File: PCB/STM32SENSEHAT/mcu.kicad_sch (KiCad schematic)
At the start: 30 parts, among them J1 USB_B_Micro, J5 Conn_01x24_Pin, J6 Conn_01x10_Pin, J7 Conn_01x05_Pin, J8 Conn_01x24_Pin, SW1 SW_Push, U6 CAT24C256, U9 FT234XD-R, U9 STLINK_UCT

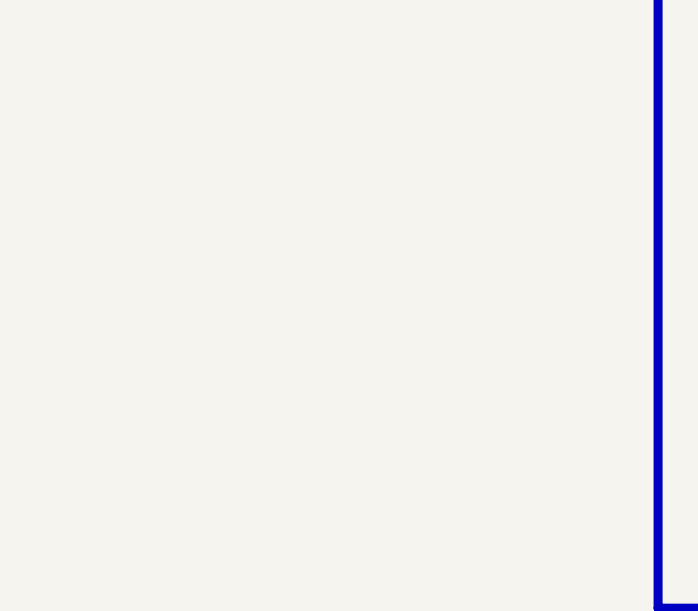
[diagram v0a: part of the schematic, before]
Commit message: OScillator added
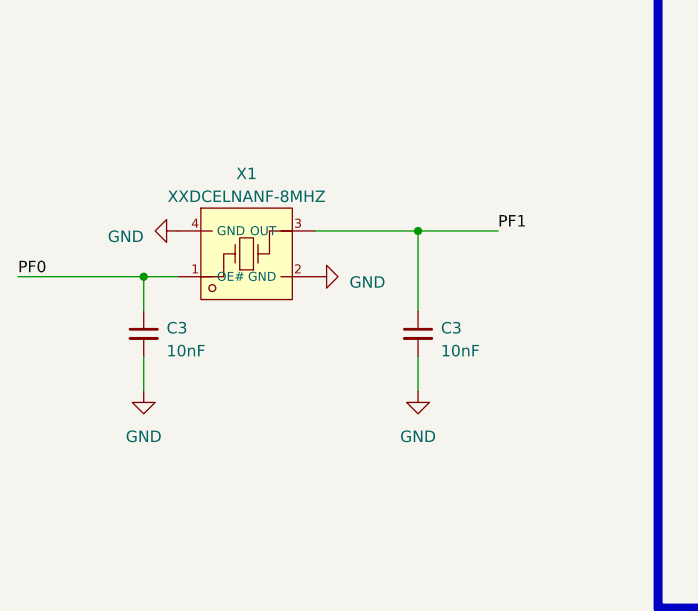
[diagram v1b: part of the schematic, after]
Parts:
- added C3 (x2): 10nF, Capacitor_SMD:C_0805_2012Metric, symbol Device:C_Small
- added X1: XXDCELNANF-8MHZ, JLCfootprint:OSC-SMD_4P-L3.2-W2.5-BL, symbol XXDCELNANF-8MHZ:XXDCELNANF-8MHZ
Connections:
- net GND: now also C3.2, C3.2, X1.2 (GND), X1.4 (GND)
- net PF0: now also C3.1, X1.1 (OE#)
- net PF1: now also C3.1, X1.3 (OUT)

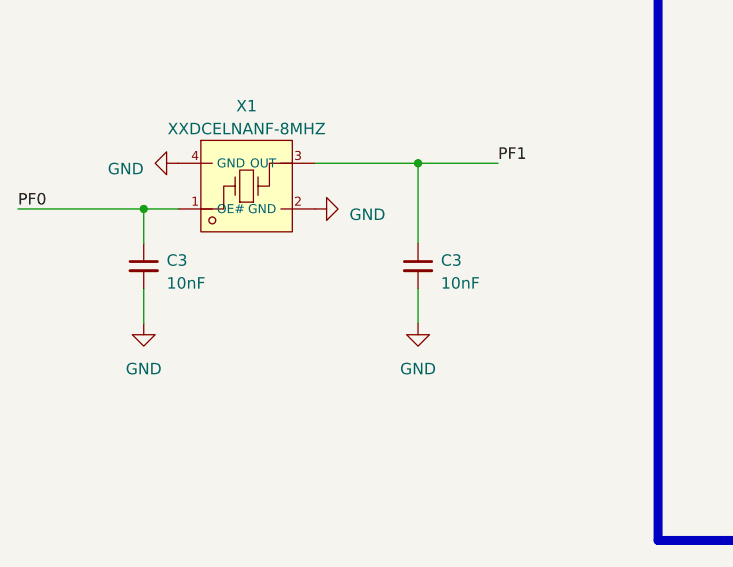
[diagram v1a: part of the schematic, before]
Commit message: Changed the value of the oscillator's capcitors to match the specified value in the datasheet
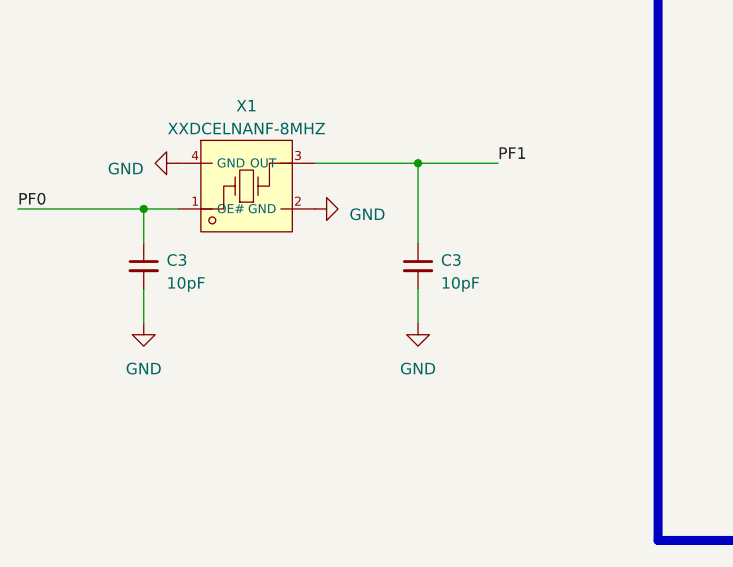
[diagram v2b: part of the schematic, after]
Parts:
- C3: value 10nF -> 10pF; footprint Capacitor_SMD:C_0805_2012Metric -> Capacitor_THT:C_Disc_D5.0mm_W2.5mm_P5.00mm
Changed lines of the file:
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@@
       (effects (font (size 1.27 1.27)) (justify left))
     )
-    (property "Value" "10nF" (at 78.74 67.9513 0)
+    (property "Value" "10pF" (at 78.74 67.9513 0)
       (effects (font (size 1.27 1.27)) (justify left))
     )
-    (property "Footprint" "Capacitor_SMD:C_0805_2012Metric" (at 76.2 66.04 0)
+    (property "Footprint" "Capacitor_THT:C_Disc_D5.0mm_W2.5mm_P5.00mm" (at 76.2 66.04 0)
       (effects (font (size 1.27 1.27)) hide)
     )
@@
       (effects (font (size 1.27 1.27)) (justify left))
     )
-    (property "Value" "10nF" (at 48.26 67.9513 0)
+    (property "Value" "10pF" (at 48.26 67.9513 0)
       (effects (font (size 1.27 1.27)) (justify left))
     )
-    (property "Footprint" "Capacitor_SMD:C_0805_2012Metric" (at 45.72 66.04 0)
+    (property "Footprint" "Capacitor_THT:C_Disc_D5.0mm_W2.5mm_P5.00mm" (at 45.72 66.04 0)
       (effects (font (size 1.27 1.27)) hide)
     )

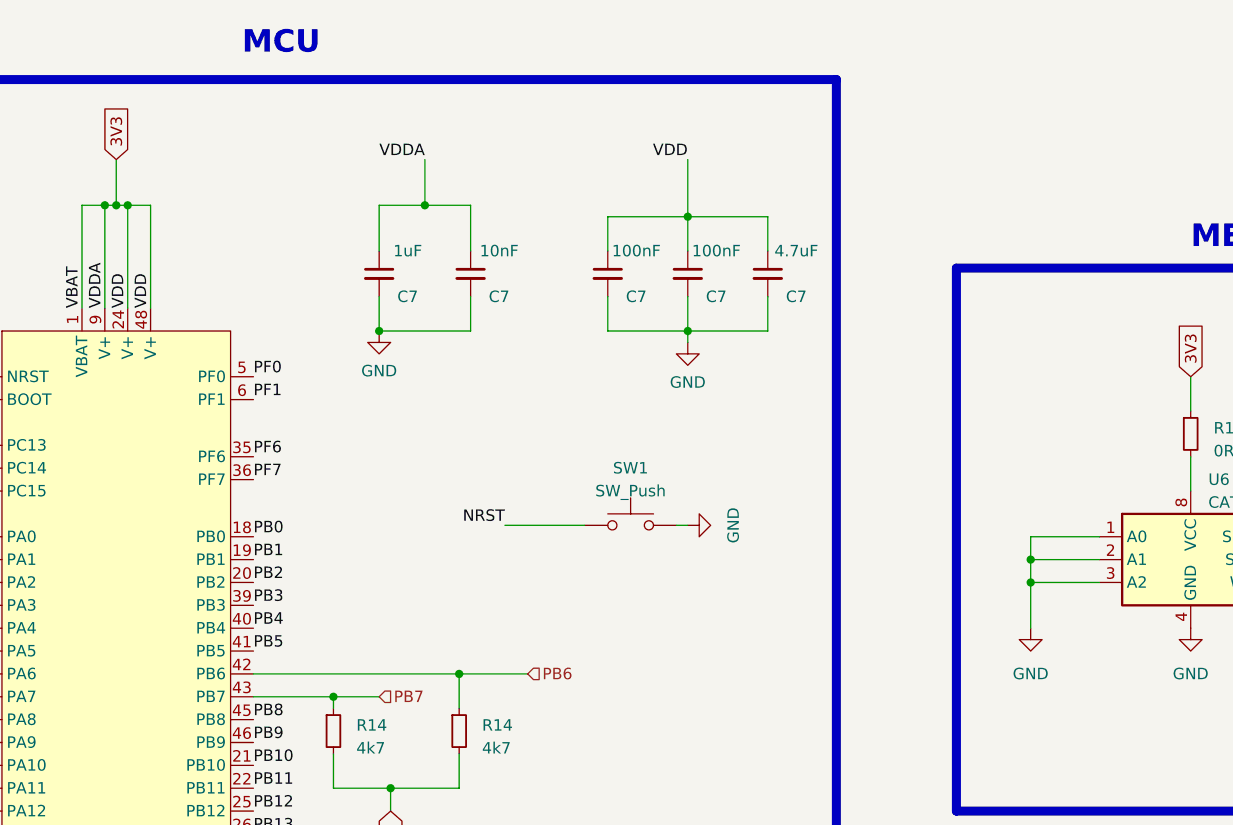
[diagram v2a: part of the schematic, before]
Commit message: Added capacitor paralle to NRST switch to mtigate parasitic effects
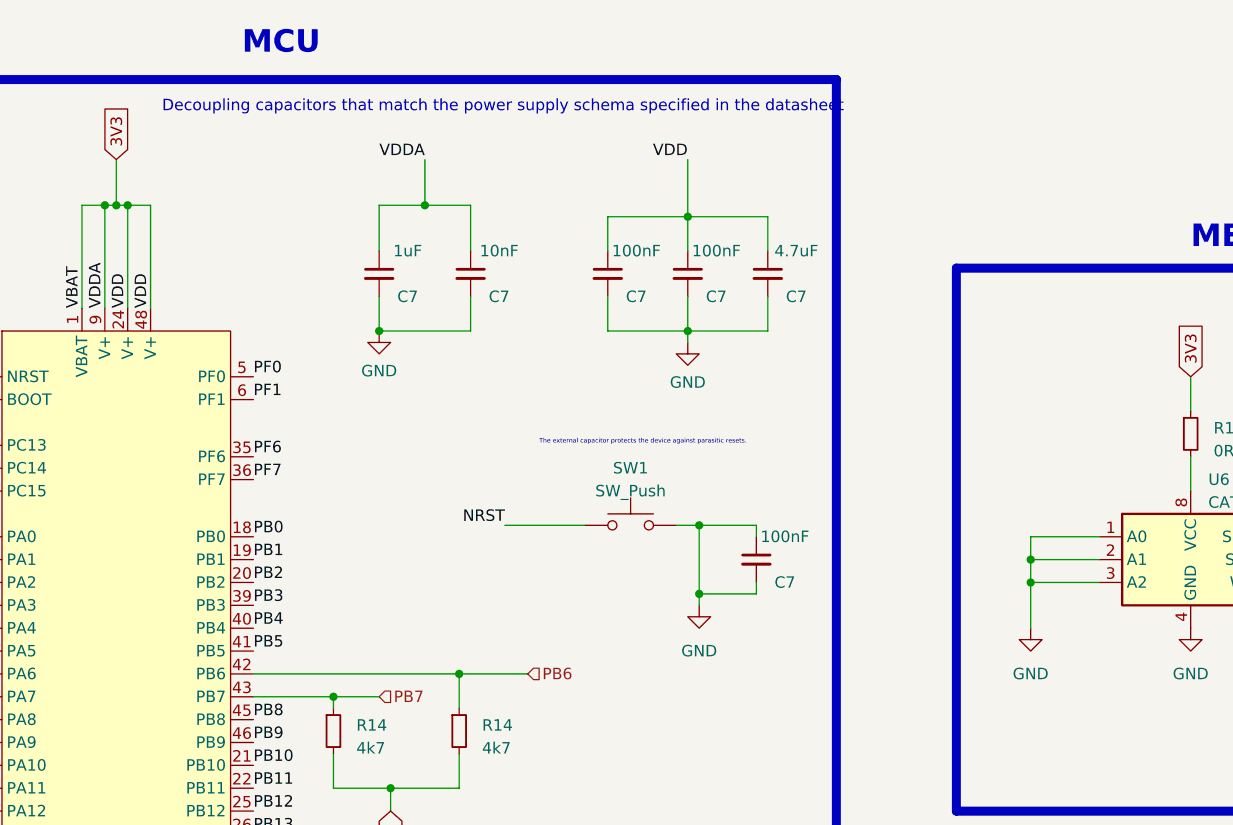
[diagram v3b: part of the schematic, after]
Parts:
- added C7: 100nF, Capacitor_THT:C_Disc_D5.0mm_W2.5mm_P5.00mm, symbol Device:C_Small
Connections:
- net GND: now also C7.1, C7.2
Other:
- note added: "Decoupling capacitors that match the power supply schema specified in the datasheet"
- note added: "The external capacitor protects the device against parasitic resets."
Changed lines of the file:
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@@
   (junction (at 228.6 119.38) (diameter 0) (color 0 0 0 0)
   )
+  (junction (at 293.37 69.85) (diameter 0) (color 0 0 0 0)
+  )
   (junction (at 330.2 76.2) (diameter 0) (color 0 0 0 0)
   )
@@
   (junction (at 330.2 73.66) (diameter 0) (color 0 0 0 0)
   )
+  (junction (at 293.37 77.47) (diameter 0) (color 0 0 0 0)
+  )
   (junction (at 228.6 34.29) (diameter 0) (color 0 0 0 0)
   )
@@
     (stroke (width 0) (type default))
   )
+  (wire (pts (xy 299.72 69.85) (xy 293.37 69.85))
+    (stroke (width 0) (type default))
+  )
   (wire (pts (xy 142.24 154.94) (xy 158.75 154.94))
     (stroke (width 0) (type default))
   )
+  (wire (pts (xy 299.72 77.47) (xy 293.37 77.47))
+    (stroke (width 0) (type default))
+  )
   (wire (pts (xy 351.79 194.31) (xy 359.41 194.31))
     (stroke (width 0) (type default))
@@
     (stroke (width 0) (type default))
   )
+  (wire (pts (xy 299.72 76.2) (xy 299.72 77.47))
+    (stroke (width 0) (type default))
+  )
   (wire (pts (xy 358.14 76.2) (xy 369.57 76.2))
     (stroke (width 0) (type default))
@@
     (stroke (width 0) (type default))
   )
+  (wire (pts (xy 293.37 77.47) (xy 293.37 69.85))
+    (stroke (width 0) (type default))
+  )
   (wire (pts (xy 208.28 101.6) (xy 213.36 101.6))
     (stroke (width 0) (type default))
@@
     (stroke (width 0) (type default))
   )
+  (wire (pts (xy 293.37 78.74) (xy 293.37 77.47))
+    (stroke (width 0) (type default))
+  )
   (wire (pts (xy 266.7 99.06) (xy 266.7 95.25))
     (stroke (width 0) (type default))
@@
     (stroke (width 0) (type default))
   )
-  (wire (pts (xy 208.28 76.2) (xy 213.36 76.2))
+  (wire (pts (xy 299.72 71.12) (xy 299.72 69.85))
     (stroke (width 0) (type default))
   )
-  (wire (pts (xy 292.1 69.85) (xy 290.83 69.85))
+  (wire (pts (xy 208.28 76.2) (xy 213.36 76.2))
     (stroke (width 0) (type default))
   )
@@
     (stroke (width 0) (type default))
   )
+  (wire (pts (xy 293.37 69.85) (xy 290.83 69.85))
+    (stroke (width 0) (type default))
+  )
   (wire (pts (xy 229.87 34.29) (xy 232.41 34.29))
     (stroke (width 0) (type default))
@@
     (effects (font (size 1.27 1.27)) (justify left top))
   )
+  (text "Decoupling capacitors that match the power supply schema specified in the datasheet"
+    (at 233.68 24.13 0)
+    (effects (font (size 1.27 1.27)) (justify left bottom))
+  )
   (text "UCT ST-LINK" (at 129.54 17.78 0)
     (effects (font (size 2.5 2.5) (thickness 0.5) bold) (justify left bottom))
   )
+  (text "The external capacitor protects the device against parasitic resets."
+    (at 275.59 60.96 0)
+    (effects (font (size 0.5 0.5)) (justify left bottom))
+  )
   (text "MCU" (at 242.57 17.78 0)
     (effects (font (size 2.5 2.5) (thickness 0.5) bold) (justify left bottom))
@@
     )
   )
-  (symbol (lib_id "power:GND") (at 292.1 69.85 90) (unit 1)
+  (symbol (lib_id "power:GND") (at 293.37 78.74 0) (unit 1)
     (in_bom yes) (on_board yes) (dnp no)
-    (property "Reference" "#PWR039" (at 298.45 69.85 0)
+    (property "Reference" "#PWR039" (at 293.37 85.09 0)
       (effects (font (size 1.27 1.27)) hide)
     )
-    (property "Value" "GND" (at 297.18 69.85 0)
+    (property "Value" "GND" (at 293.37 83.82 0)
       (effects (font (size 1.27 1.27)))
     )
-    (property "Footprint" "" (at 292.1 69.85 0)
+    (property "Footprint" "" (at 293.37 78.74 0)
       (effects (font (size 1.27 1.27)) hide)
     )
-    (property "Datasheet" "" (at 292.1 69.85 0)
+    (property "Datasheet" "" (at 293.37 78.74 0)
       (effects (font (size 1.27 1.27)) hide)
     )
@@
         )
       )
+    )
+  )
+  (symbol (lib_id "Device:C_Small") (at 299.72 73.66 0) (unit 1)
+    (in_bom yes) (on_board yes) (dnp no)
+    (property "Reference" "C7" (at 302.895 76.2 0)
+      (effects (font (size 1.27 1.27)))
+    )
+    (property "Value" "100nF" (at 302.895 71.12 0)
+      (effects (font (size 1.27 1.27)))
+    )
+    (property "Footprint" "Capacitor_THT:C_Disc_D5.0mm_W2.5mm_P5.00mm" (at 299.72 73.66 0)
+      (effects (font (size 1.27 1.27)) hide)
+    )
+    (property "Datasheet" "~" (at 299.72 73.66 0)
+      (effects (font (size 1.27 1.27)) hide)
+    )
+    (property "Basic" "" (at 299.72 73.66 0)
+      (effects (font (size 1.27 1.27)) hide)
+    )
+    (property "DNP" "" (at 299.72 73.66 0)
+      (effects (font (size 1.27 1.27)) hide)
+    )
+    (property "Extended" "" (at 299.72 73.66 0)
+      (effects (font (size 1.27 1.27)) hide)
+    )
+    (property "MOQ and Attrition" "" (at 299.72 73.66 0)
+      (effects (font (size 1.27 1.27)) hide)
+    )
+    (property "Price" "" (at 299.72 73.66 0)
+      (effects (font (size 1.27 1.27)) hide)
+    )
+    (pin "1")
+    (pin "2")
+    (instances
+      (project "STM32SENSEHAT"
+        (path "/e47212d5-bd6f-4bb8-9ec7-12aac08f34b5/e2c75964-4e94-4a3b-9ddf-38bb01f2971b"
+          (reference "C7") (unit 1)
+        )
+        (path "/e47212d5-bd6f-4bb8-9ec7-12aac08f34b5/8fedf9e5-f663-4f34-96fe-3613b2b14be8"
+          (reference "C19") (unit 1)
+        )
+      )

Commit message: Added a poer indicator LED and rectified NRST parastic capacitance
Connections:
- net GND: no longer C7.1
- net NRST: now also C7.1
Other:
- moved on the sheet: C3, X1

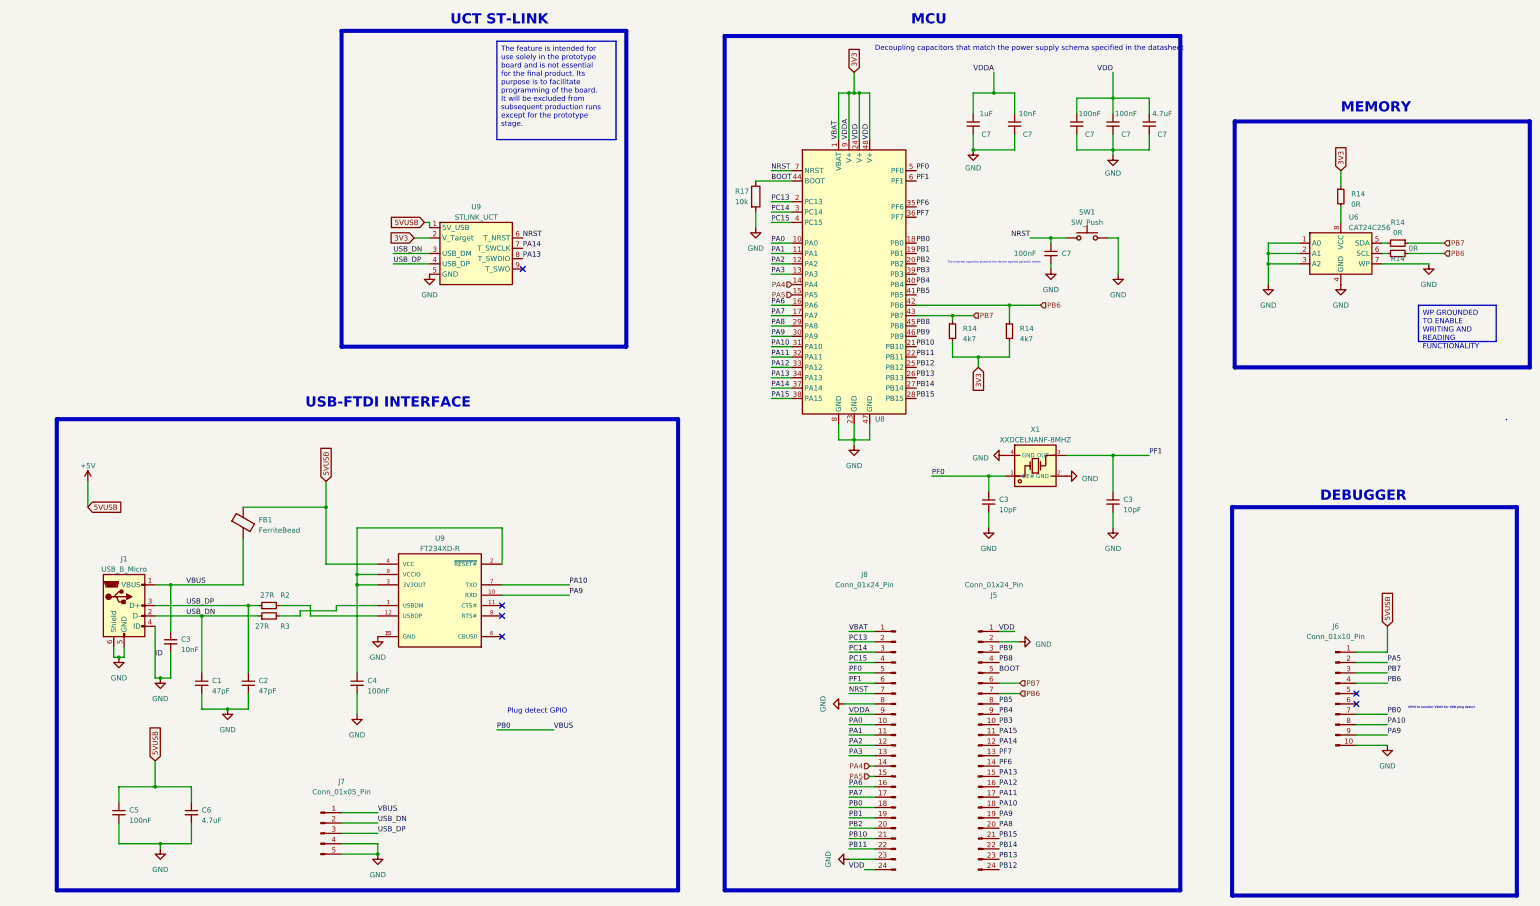
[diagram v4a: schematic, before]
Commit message: Changed the QR Code on PCB
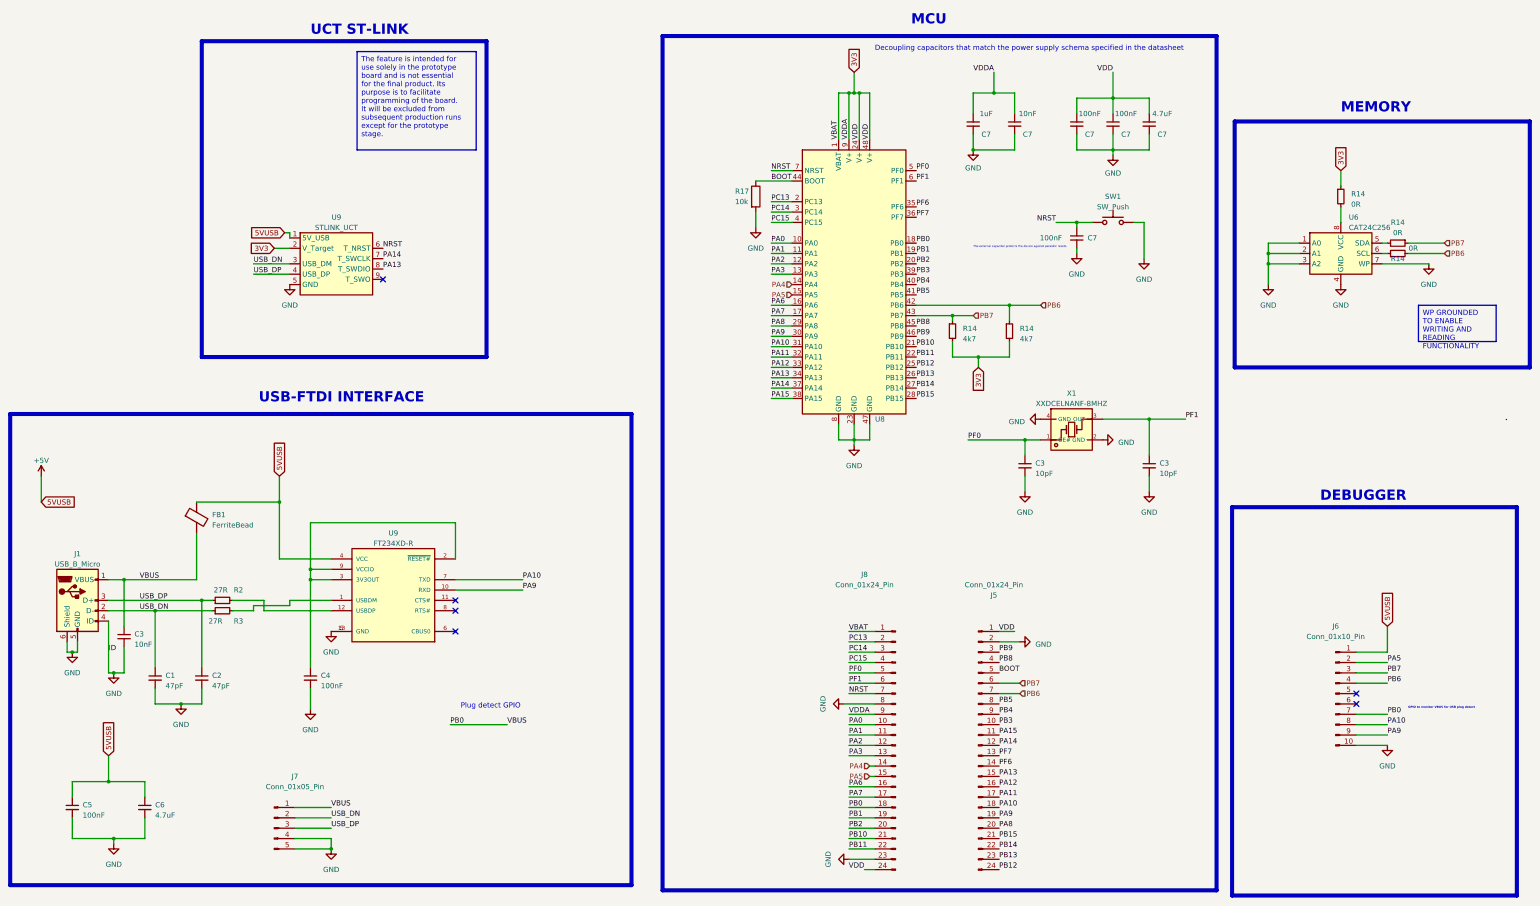
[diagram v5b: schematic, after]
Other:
- moved on the sheet: C1, C2, C3, C4, C5, C6, C7, FB1, J1, J7, R2, R3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
